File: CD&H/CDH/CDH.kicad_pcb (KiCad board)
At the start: 2 copper layers, 96 x 90 mm, 24 parts, among them J1 THD-20-R, J4 USB_OTG, U1 74LVC1G07SE-7, U1 ATA6560-GAQW-VAO, U2 TPD2EUSB30, U3 MCP2510-E/SO, U4 74LVC1G07SE-7

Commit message: updates
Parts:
- added P1: S04B-PASK-2(LF)(SN), S04B-PASK-2_LF__SN_:JST_S04B-PASK-2(LF)(SN), F.Cu at (131.6, 64.5)
- added P2: S04B-PASK-2(LF)(SN), S04B-PASK-2_LF__SN_:JST_S04B-PASK-2(LF)(SN), F.Cu at (146.2, 64.6)
- Module1: value ComputeModule4-CM4 -> DF40GB-10DP-0.4V(51)
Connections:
- J1 pad 10: /CM4 GPIO/GPIO15 -> (no net)
- J1 pad 8: /CM4 GPIO/GPIO14 -> (no net)
- Module1 pad 191: GND -> /CM4 GPIO/GPIO13
- Module1 pad 192: GND -> /CM4 GPIO/GPIO12
- U3 pad 12: /CM4 GPIO/GPIO12 -> unconnected-(U3-Pad12)
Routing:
- net /CM4 GPIO/GPIO12: track 0.00 -> 43.9 mm, vias 0 -> 3
- net +5V: track 137.1 -> 178.6 mm
- net /CM4 GPIO/GPIO13: track 0.00 -> 39.5 mm, vias 0 -> 1
- net /CM4 GPIO/GPIO14: track 52.2 -> 42.4 mm, vias 4 -> 1
- net /CM4 GPIO/GPIO15: track 51.2 -> 42.2 mm, vias 4 -> 1
- net GND: track 210.2 -> 210.3 mm, vias 17 -> 19
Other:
- board text removed: "RPi CM4 Base Carrier"

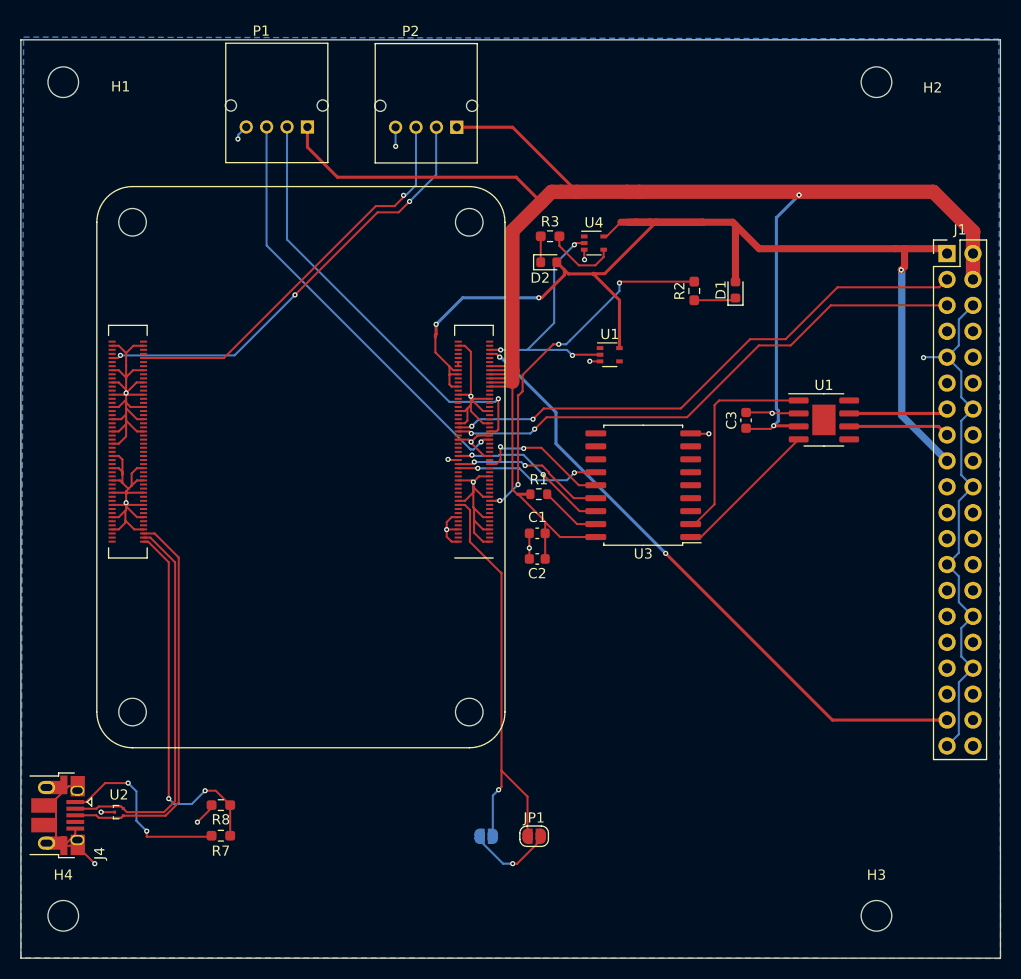
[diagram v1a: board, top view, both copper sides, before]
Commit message: modifications for v2
CDH: UART connector relocation, LED relocation, removed EEPROM solder jumper
Payload: Removed connection to GND of unconnected ground-plane pins, adjusted traces
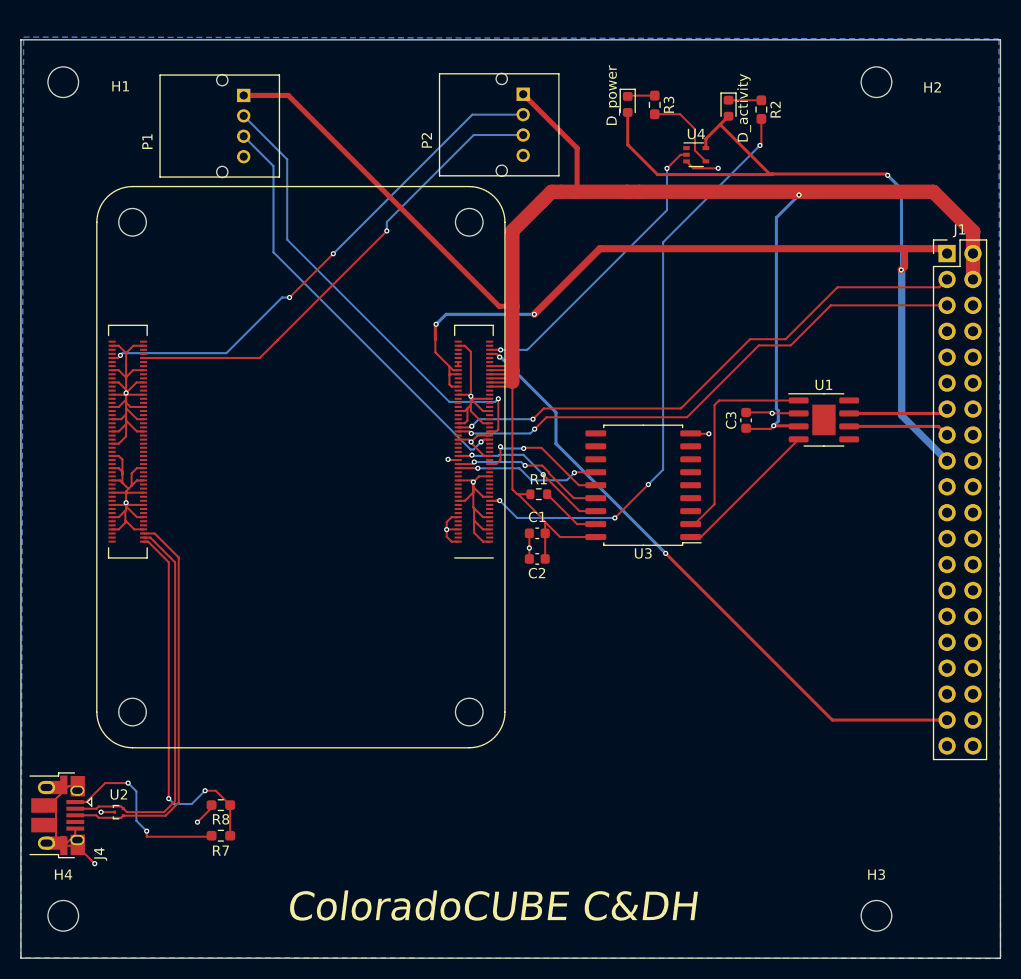
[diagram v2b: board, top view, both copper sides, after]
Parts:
- removed JP1 (x2): SolderJumper_2_Open, Jumper:SolderJumper-2_P1.3mm_Open_RoundedPad1.0x1.5mm
- removed the U1 at (164.2, 86.9)
- moved R2 18.9 mm to (179.1, 62.8), turned to -90 degrees
- moved D_activity 17.8 mm to (175.8, 62.7), turned to -90 degrees
- moved D_power 17.3 mm to (166.0, 62.3), turned to -90 degrees
- moved R3 16.5 mm to (168.6, 62.4), turned to -90 degrees
- moved U4 13.2 mm to (172.7, 67.3)
- moved P2 9.51 mm to (155.7, 64.3), turned to 90 degrees
- moved P1 3.25 mm to (128.3, 64.5), turned to 90 degrees
- renumbered D1 to D_activity, D2 to D_power
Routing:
- net GND: track 210.3 -> 146.9 mm, vias 19 -> 14
- net /CM4 GPIO/EEPROM_nWP: track 42.8 -> 0.00 mm, vias 1 -> 0
- net /CM4 GPIO/nLED_Activity: track 35.5 -> 58.0 mm
- net +3.3V: track 116.3 -> 136.7 mm, vias 3 -> 4
- net /CM4 GPIO/GPIO13: track 39.5 -> 46.9 mm
- net /CM4 GPIO/GPIO12: track 43.9 -> 50.2 mm
- net /CM4 GPIO/nPWR_LED: track 24.4 -> 29.6 mm, vias 3 -> 2
- net +5V: track 178.6 -> 183.9 mm
- net /CM4 GPIO/GPIO14: track 42.4 -> 45.2 mm
- net Net-(R3-Pad2): track 7.13 -> 8.15 mm
- net Net-(D1-Pad1): track 4.13 -> 3.23 mm
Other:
- board text added: "ColoradoCUBE C&DH"
